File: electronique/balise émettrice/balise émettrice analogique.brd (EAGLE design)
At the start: 74.9 x 74.9 mm, 53 parts, among them IC1 TL084P, IC2 TL084P, J1 J7MM

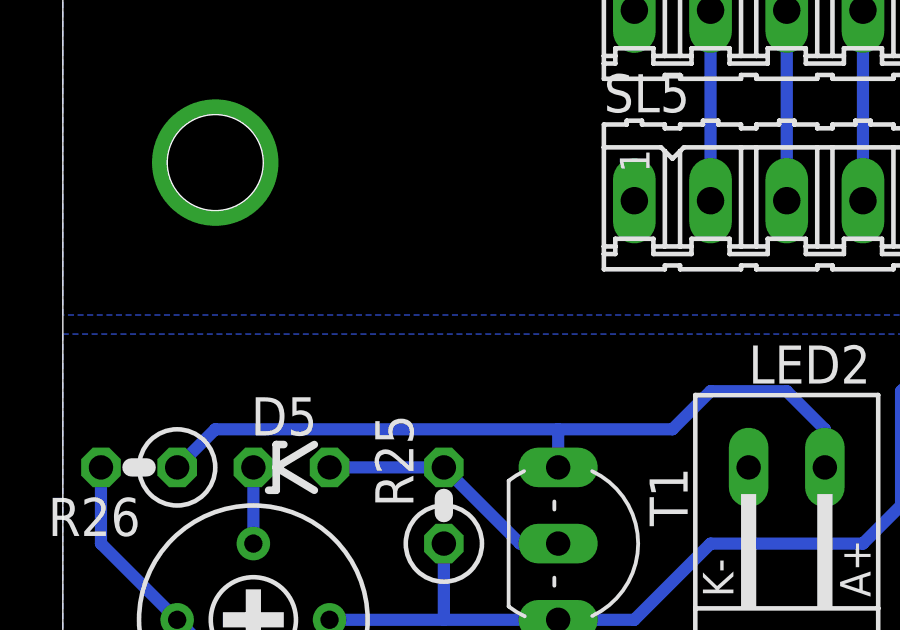
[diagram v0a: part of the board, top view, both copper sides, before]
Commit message: correctif equations des filtres + ajout debut circuit de reception
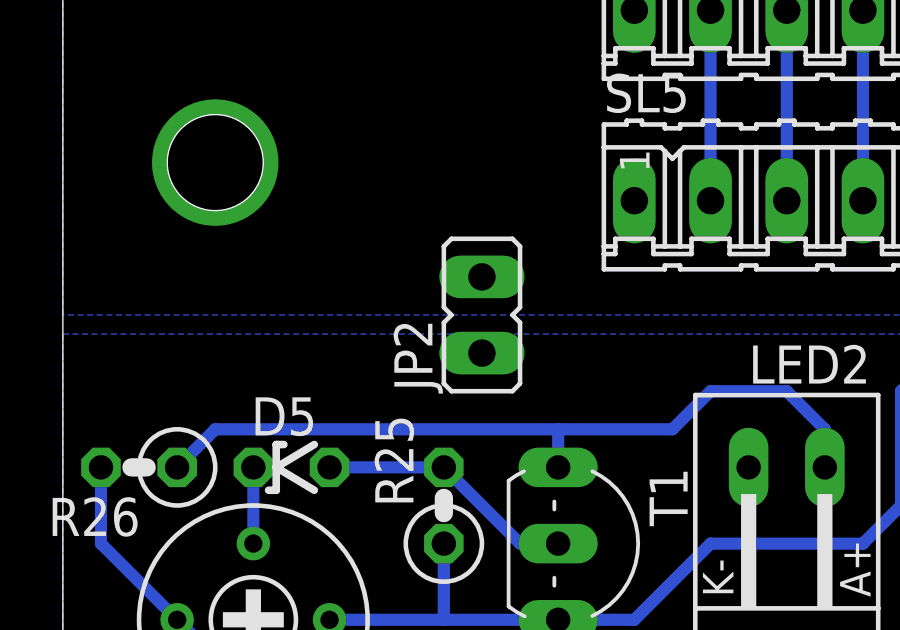
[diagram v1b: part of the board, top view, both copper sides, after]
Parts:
- added JP2: (no value), jumper:JP1
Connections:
- net 0V: now also JP2.1
- net GND: now also JP2.2
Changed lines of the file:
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@@
 <attribute name="OC_FARNELL" value="unknown" x="26.67" y="24.13" size="1.778" layer="27" display="off"/>
 </element>
+<element name="JP2" library="jumper" package="JP1" value="" x="13.97" y="13.97"/>
 </elements>
 <signals>
@@
 <via x="69.85" y="69.85" extent="1-16" drill="3.2"/>
 <via x="5.08" y="19.05" extent="1-16" drill="3.2"/>
+<contactref element="JP2" pad="2"/>
 </signal>
 <signal name="N$6">
@@
 <vertex x="0" y="0"/>
 </polygon>
+<contactref element="JP2" pad="1"/>
 </signal>
 <signal name="N$11">

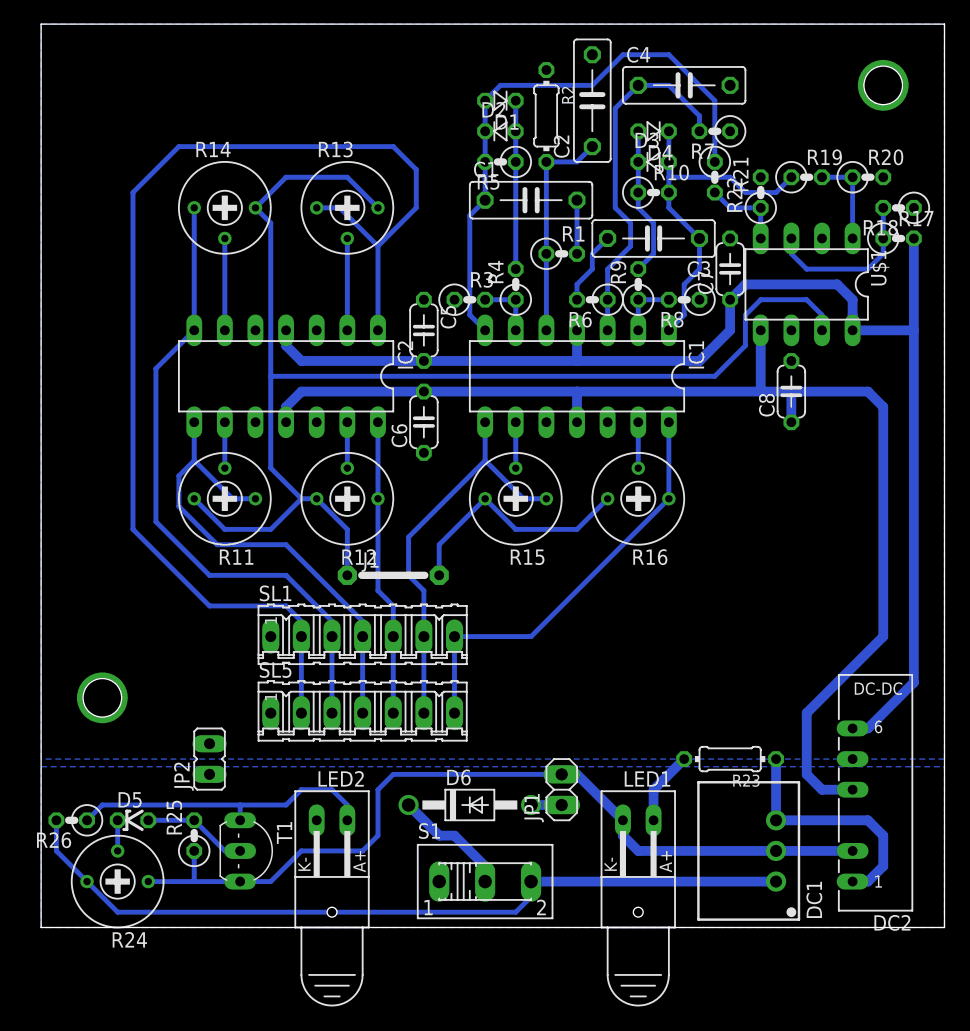
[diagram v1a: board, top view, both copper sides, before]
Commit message: maj filtrage + ajout routage balise receptrice, partie filtrage
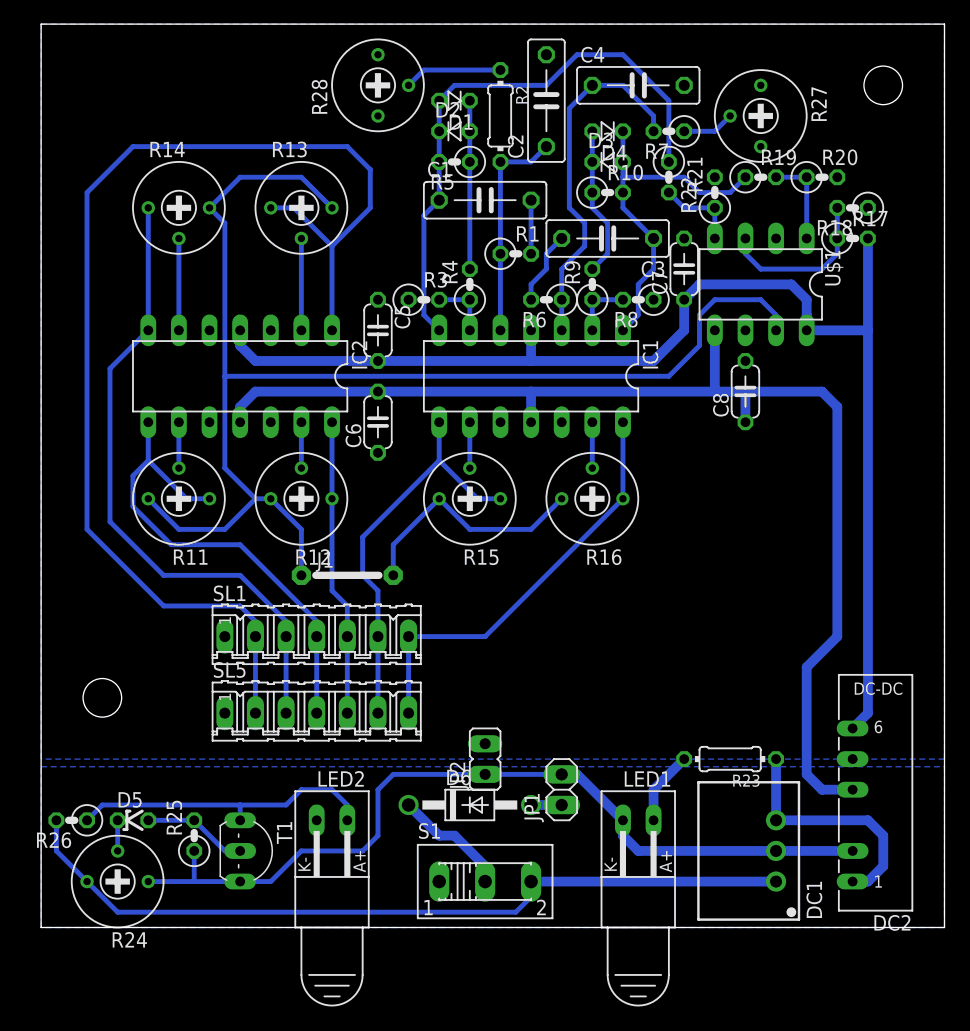
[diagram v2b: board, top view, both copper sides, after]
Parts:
- added R27: 10K, resistor:RTRIM3339P
- added R28: 2K, resistor:RTRIM3339P
- R7: value 18K -> 8K2
- moved JP2 22.9 mm to (36.8, 14.0)
- moved C1 3.81 mm to (36.8, 60.3)
- moved C2 3.81 mm to (41.9, 68.6)
- moved C4 3.81 mm to (49.5, 69.8)
- moved D1 3.81 mm to (34.3, 68.6)
- moved D2 3.81 mm to (34.3, 66.0)
- moved IC1 3.81 mm to (40.6, 45.7)
- moved J1 3.81 mm to (25.4, 29.2)
- moved R1 3.81 mm to (39.4, 55.9)
- moved R16 3.81 mm to (45.7, 35.6)
- moved R17 3.81 mm to (67.3, 57.1)
- moved R18 3.81 mm to (67.3, 59.7)
- moved R19 3.81 mm to (59.7, 62.2)
- moved R20 3.81 mm to (64.8, 62.2)
- moved R22 3.81 mm to (52.1, 62.2)
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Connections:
- new net N$26: R27.2, R7.1
- new net N$27: R2.1, R28.2
- net GND: now also R27.1, R28.1; no longer R2.1, R7.1
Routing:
- net N$27: track 0.00 -> 8.15 mm
- net N$26: track 0.00 -> 4.34 mm
- net +15V: track 108.3 -> 106.0 mm
- net -15V: track 99.5 -> 97.9 mm

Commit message: maj balise emettrice : ajout de la DEL de debug + interrupteur dans le modele 3D
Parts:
- removed S1: (no value), switch:255SB
- added U$2: 1RT, switch:1RT
- moved R25 2.84 mm to (14.0, 10.2)
- moved T1 2.84 mm to (17.8, 8.89)
- moved D5 2.84 mm to (8.89, 11.4)
- moved R24 2.84 mm to (7.62, 6.35)
- moved R26 2.84 mm to (3.81, 11.4)
- moved DC1 1.27 mm to (61.0, 7.62)
- moved R23 1.27 mm to (57.1, 15.2)
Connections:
- net +9V: now also U$2.3; no longer S1.3
- net N$23: now also U$2.2; no longer S1.2
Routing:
- net 0V: track 72.8 -> 14.5 mm
- net N$14: track 6.13 -> 7.40 mm
- net N$22: track 25.7 -> 24.4 mm
- net N$23: track 9.72 -> 10.4 mm
- net N$11: track 20.1 -> 20.6 mm

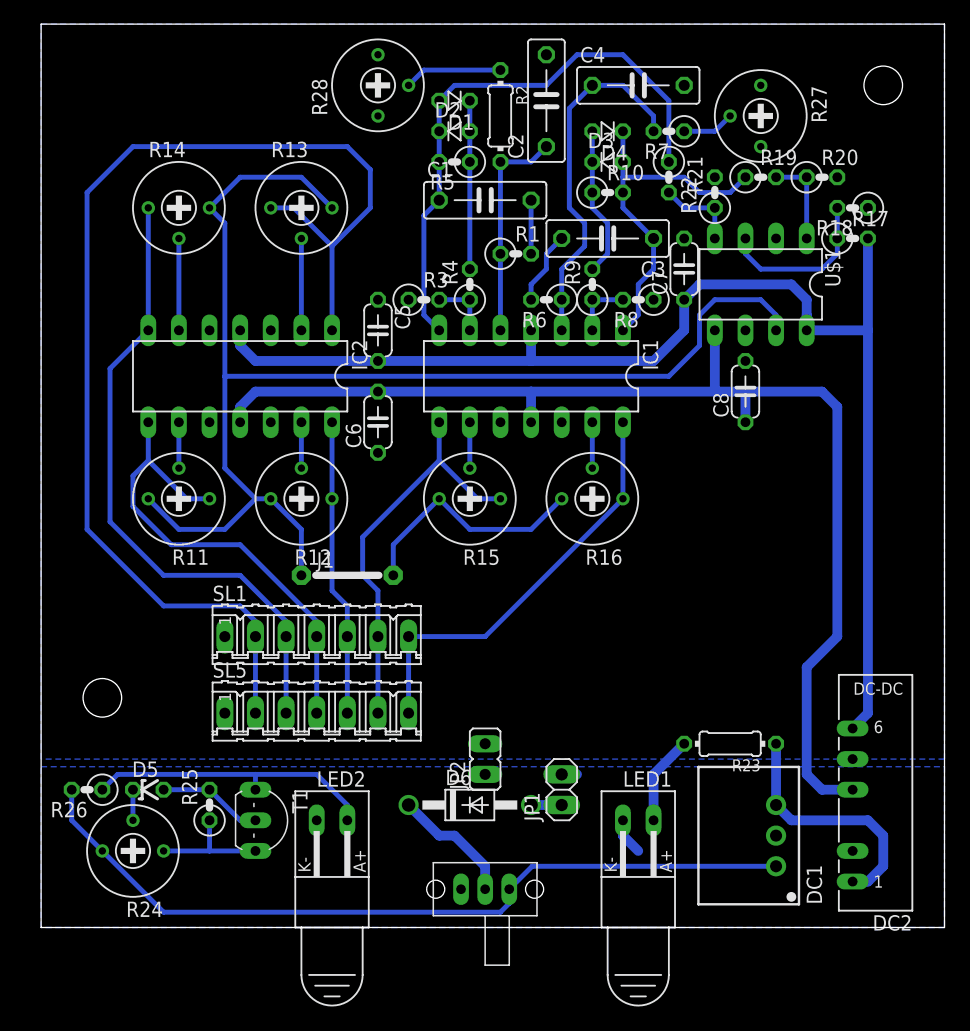
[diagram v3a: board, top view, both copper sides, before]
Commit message: maj mineure elec + ajout doc de l'elec
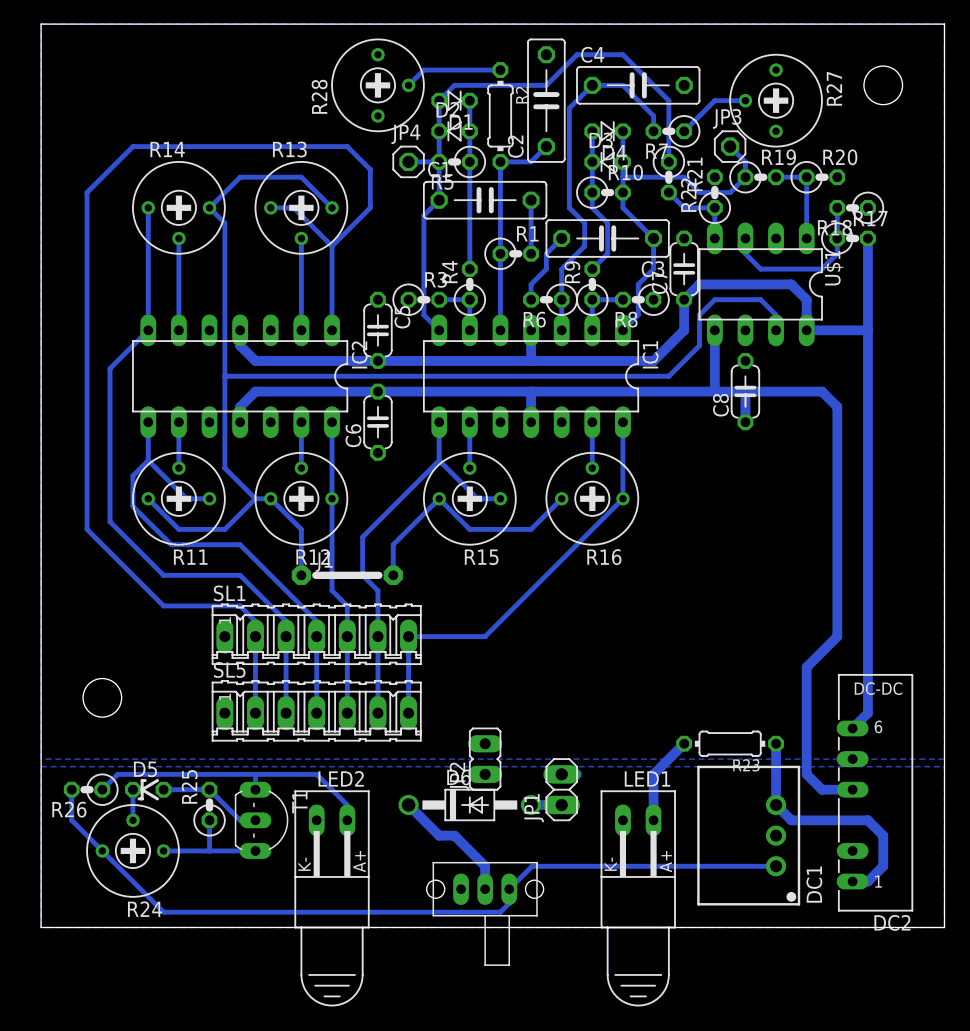
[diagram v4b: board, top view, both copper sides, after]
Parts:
- added JP3, JP4: (no value), pinhead:1X01
- moved R27 1.80 mm to (61.0, 68.6)
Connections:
- net 40-80HZ: now also JP4.1
- net 40KHZ: now also JP3.1
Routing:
- net 0V: track 14.5 -> 11.4 mm
- net 40KHZ: track 29.8 -> 32.9 mm
- net 40-80HZ: track 47.4 -> 49.9 mm
- net N$26: track 4.34 -> 6.13 mm
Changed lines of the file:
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@@
 <setting verticaltext="up"/>
 </settings>
-<grid distance="0.05" unitdist="inch" unit="mm" style="lines" multiple="1" display="yes" altdistance="0.025" altunitdist="inch" altunit="inch"/>
+<grid distance="0.05" unitdist="inch" unit="inch" style="lines" multiple="1" display="yes" altdistance="0.025" altunitdist="inch" altunit="inch"/>
 <layers>
 <layer number="1" name="Top" color="4" fill="1" visible="yes" active="yes"/>
@@
 <attribute name="MPN" value="" x="36.83" y="13.97" size="1.778" layer="27" display="off"/>
 </element>
-<element name="R27" library="resistor" package="RTRIM3339P" value="10K" x="59.69" y="67.31" rot="R270">
-<attribute name="OC_FARNELL" value="unknown" x="59.69" y="67.31" size="1.778" layer="27" rot="R270" display="off"/>
-<attribute name="MF" value="" x="59.69" y="67.31" size="1.778" layer="27" rot="R270" display="off"/>
-<attribute name="MPN" value="" x="59.69" y="67.31" size="1.778" layer="27" rot="R270" display="off"/>
+<element name="R27" library="resistor" package="RTRIM3339P" value="10K" x="60.96" y="68.58" rot="R270">
+<attribute name="OC_FARNELL" value="unknown" x="60.96" y="68.58" size="1.778" layer="27" rot="R270" display="off"/>
+<attribute name="MF" value="" x="60.96" y="68.58" size="1.778" layer="27" rot="R270" display="off"/>
+<attribute name="MPN" value="" x="60.96" y="68.58" size="1.778" layer="27" rot="R270" display="off"/>
 </element>
 <element name="R28" library="resistor" package="RTRIM3339P" value="2K" x="27.94" y="69.85" rot="R90">
@@
 </element>
 <element name="U$2" library="switch" package="1RT" value="1RT" x="36.83" y="3.175"/>
+<element name="JP3" library="pinhead" package="1X01" value="" x="57.15" y="64.77"/>
+<element name="JP4" library="pinhead" package="1X01" value="" x="30.48" y="63.5"/>
 </elements>
 <signals>
@@
 <wire x1="54.61" y1="60.96" x2="53.34" y2="62.23" width="0.4064" layer="16"/>
 <wire x1="53.34" y1="62.23" x2="48.26" y2="62.23" width="0.4064" layer="16"/>
+<contactref element="JP3" pad="1"/>
+<wire x1="57.15" y1="64.77" x2="58.42" y2="63.5" width="0.4064" layer="16"/>
+<wire x1="58.42" y1="63.5" x2="58.42" y2="62.23" width="0.4064" layer="16"/>
 </signal>
 <signal name="N$9">
@@
 <wire x1="41.91" y1="69.85" x2="34.29" y2="69.85" width="0.4064" layer="16"/>
 <wire x1="34.29" y1="69.85" x2="33.02" y2="68.58" width="0.4064" layer="16"/>
+<contactref element="JP4" pad="1"/>
+<wire x1="30.48" y1="63.5" x2="33.02" y2="63.5" width="0.4064" layer="16"/>
 </signal>
 <signal name="N$4">
@@
 <contactref element="JP1" pad="2"/>
 <wire x1="43.18" y1="12.7" x2="44.45" y2="12.7" width="0.8128" layer="16"/>
-<wire x1="48.26" y1="8.89" x2="48.26" y2="7.62" width="0.8128" layer="16"/>
-<wire x1="48.26" y1="7.62" x2="49.53" y2="6.35" width="0.8128" layer="16"/>
 <wire x1="17.78" y1="6.35" x2="13.97" y2="6.35" width="0.4064" layer="16"/>
 <wire x1="13.97" y1="6.35" x2="10.16" y2="6.35" width="0.4064" layer="16"/>
@@
 <contactref element="R7" pad="1"/>
 <contactref element="R27" pad="2"/>
-<wire x1="53.34" y1="66.04" x2="55.88" y2="66.04" width="0.4064" layer="16"/>
-<wire x1="55.88" y1="66.04" x2="57.15" y2="67.31" width="0.4064" layer="16"/>
+<wire x1="53.34" y1="66.04" x2="55.88" y2="68.58" width="0.4064" layer="16"/>
+<wire x1="55.88" y1="68.58" x2="58.42" y2="68.58" width="0.4064" layer="16"/>
 </signal>
 <signal name="N$27">
